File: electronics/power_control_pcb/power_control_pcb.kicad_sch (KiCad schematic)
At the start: 83 parts

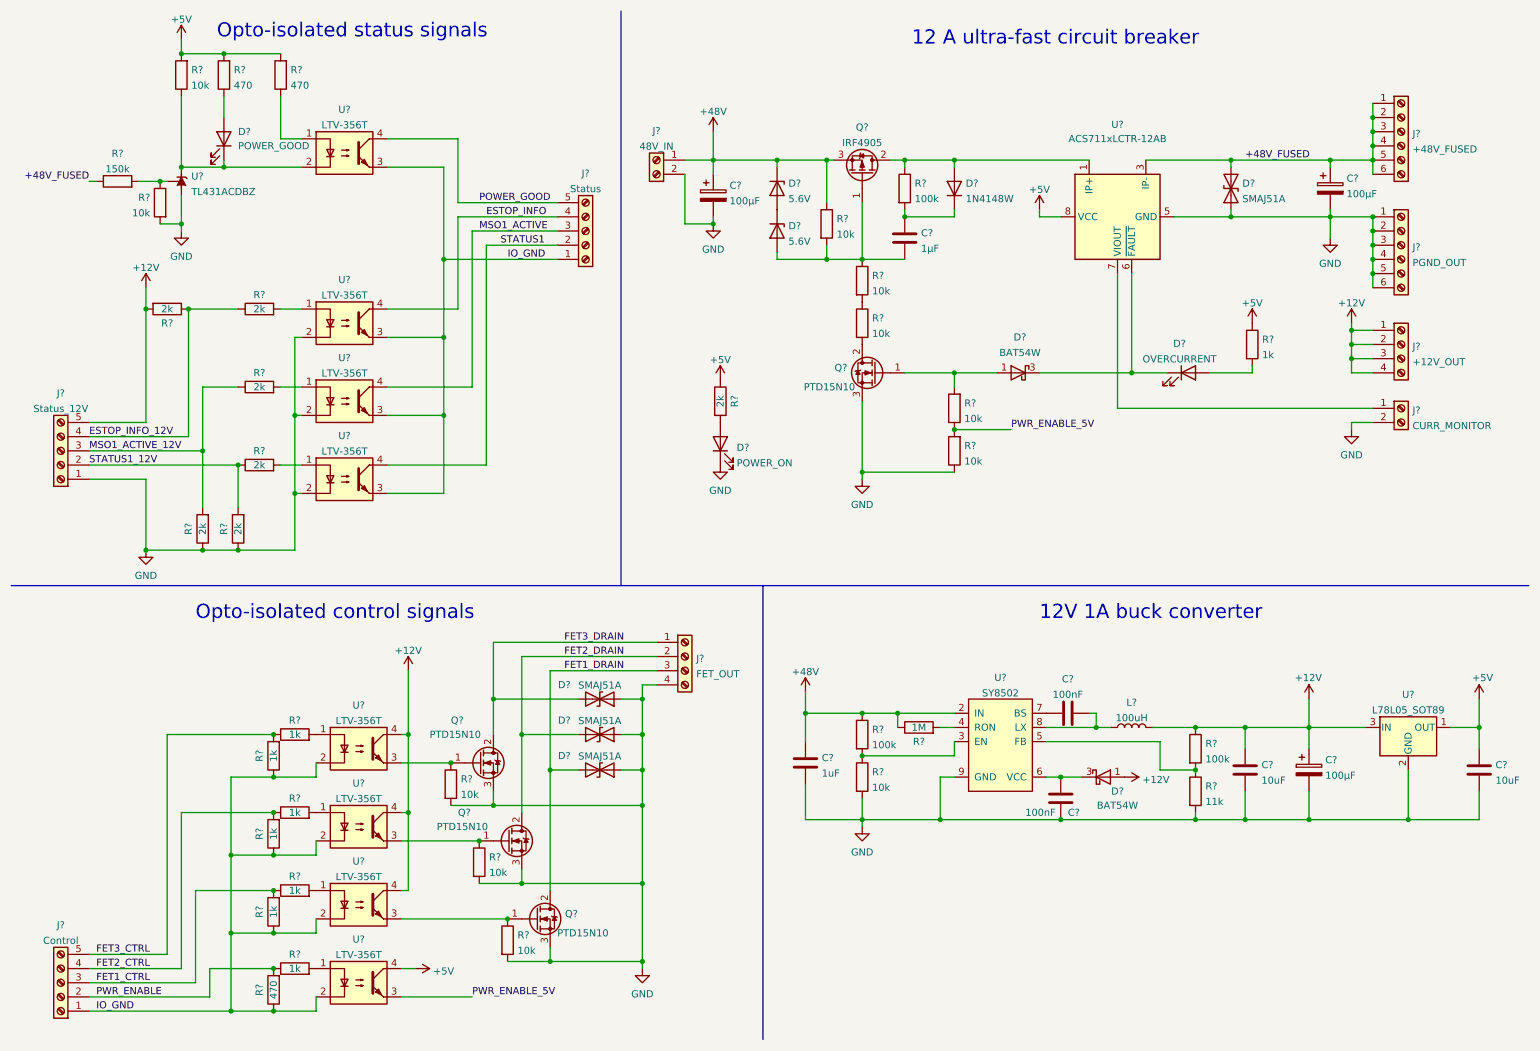
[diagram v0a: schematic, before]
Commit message: Update motor driver and power control PCB designs
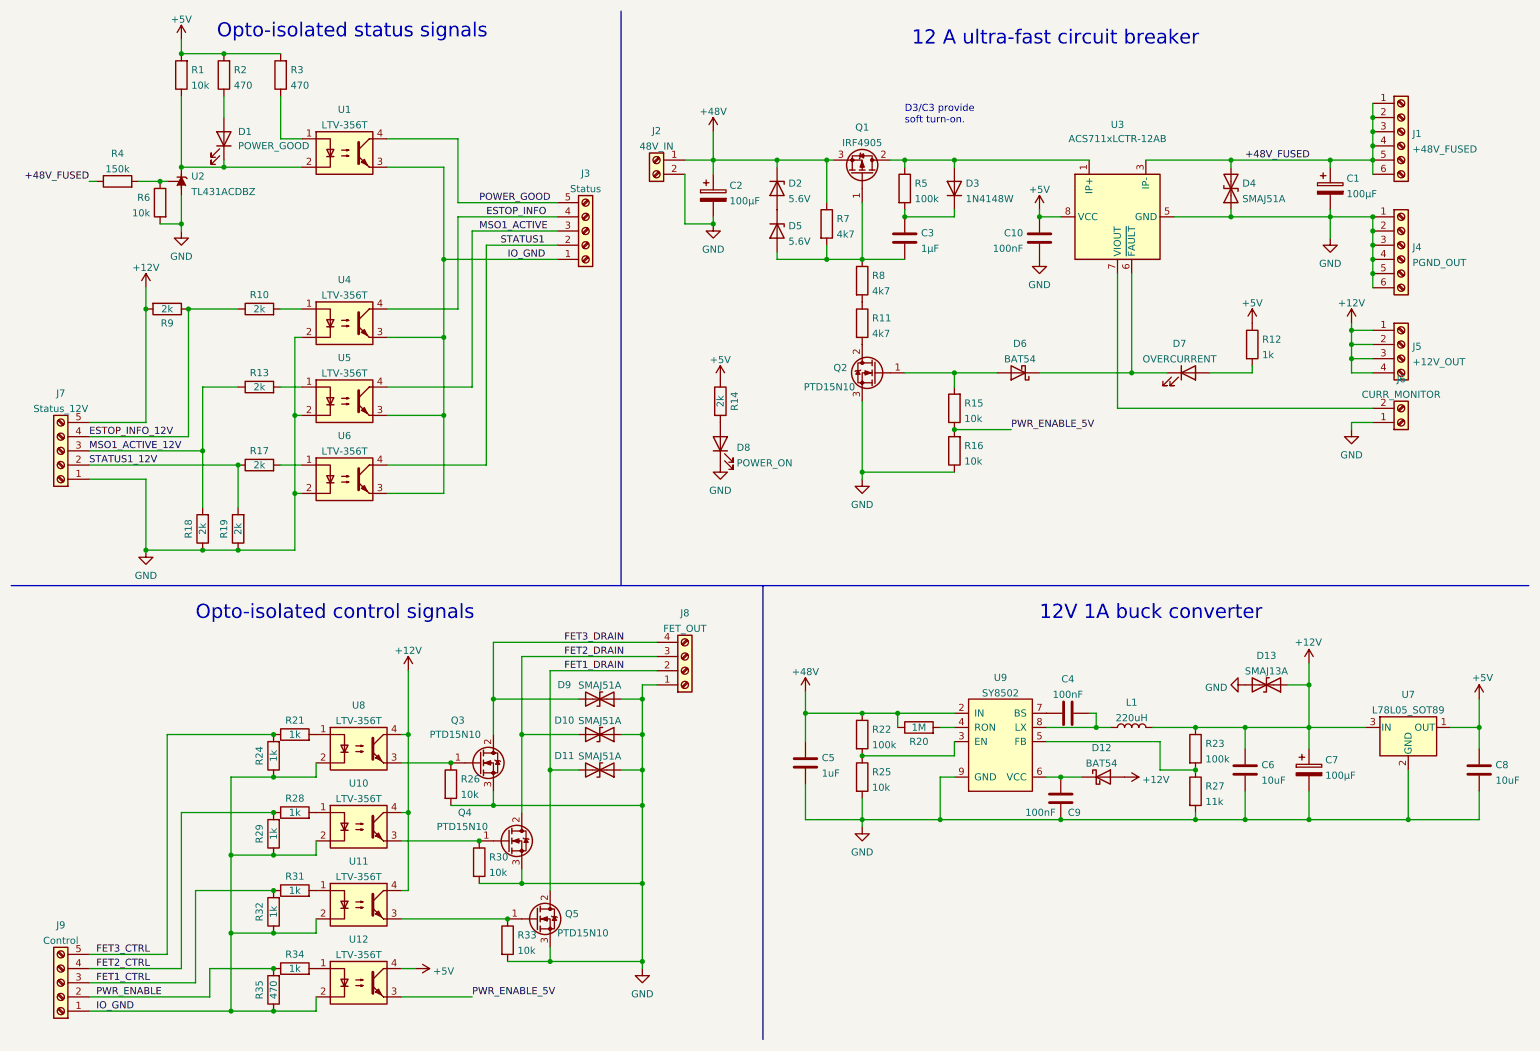
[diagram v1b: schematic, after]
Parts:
- removed D? (x2): BAT54W, Package_TO_SOT_SMD:SOT-323_SC-70, symbol Diode:BAT54W
- added C10: 100nF, Capacitor_SMD:C_0603_1608Metric, symbol Device:C
- added D12, D6: BAT54, Diode_SMD:D_SOD-123, symbol Device:D_Schottky
- added D13: SMAJ13A, Diode_SMD:D_SMA, symbol Device:D_TVS
- C1, C2, C7: renamed from C?; footprint (none) -> Capacitor_THT:CP_Radial_D10.0mm_P5.00mm
- C3, C5: renamed from C?; footprint (none) -> Capacitor_SMD:C_1210_3225Metric
- C4, C9: renamed from C?; footprint (none) -> Capacitor_SMD:C_0603_1608Metric
- C6, C8: renamed from C?; footprint (none) -> Capacitor_SMD:C_0805_2012Metric
- D1, D7, D8: renamed from D?; footprint (none) -> LED_THT:LED_D3.0mm
- D10, D11, D4, D9: renamed from D?; footprint (none) -> Diode_SMD:D_SMA
- D2, D5: renamed from D?; footprint (none) -> Diode_SMD:D_SOD-123
- J1, J4: renamed from J?; footprint (none) -> TerminalBlock_Phoenix:TerminalBlock_Phoenix_MKDS-1,5-6_1x06_P5.00mm_Horizontal
- J2, J6: renamed from J?; footprint (none) -> TerminalBlock_Phoenix:TerminalBlock_Phoenix_MKDS-1,5-2_1x02_P5.00mm_Horizontal
- J3, J7, J9: renamed from J?; footprint (none) -> TerminalBlock_TE-Connectivity:TerminalBlock_TE_282834-5_1x05_P2.54mm_Horizontal
- J5, J8: renamed from J?; footprint (none) -> TerminalBlock_Phoenix:TerminalBlock_Phoenix_MKDS-1,5-4_1x04_P5.00mm_Horizontal
- L1: renamed from L?; value 100uH -> 220uH; footprint (none) -> Inductor_SMD:L_12x12mm_H6mm
- Q1: renamed from Q?; footprint Package_TO_SOT_THT:TO-220-3_Vertical -> Package_TO_SOT_SMD:TO-263-3_TabPin2
- R1, R10, R12, R13, R14, R15, R16, R17, R18, R19, R2, R20, R21, R22, R23, R24, R25, R26, R27, R28, R29, R3, R30, R31, R32, R33, R34, R35, R4, R5, R6, R9: renamed from R?; footprint (none) -> Resistor_SMD:R_0603_1608Metric
- R11, R7, R8: renamed from R?; value 10k -> 4k7; footprint (none) -> Resistor_SMD:R_0603_1608Metric
- U9: renamed from U?; footprint (none) -> Package_SO:SOIC-8-1EP_3.9x4.9mm_P1.27mm_EP2.29x3mm
- gave numbers to parts that had none: 16
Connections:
- net +12V: now also D12.2 (A), D13.1 (A1)
- net +5V: now also C10.1
- net FET1_DRAIN: now also J8.2 (Pin_2); no longer J8.3 (Pin_3)
- net FET2_DRAIN: now also J8.3 (Pin_3); no longer J8.2 (Pin_2)
- net FET3_DRAIN: now also J8.4 (Pin_4); no longer J8.1 (Pin_1)
- net GND: now also J6.1 (Pin_1), J8.1 (Pin_1), C10.2, D13.2 (A2); no longer J6.2 (Pin_2), J8.4 (Pin_4)
- net at D7.1 (K), U3.6 (~{FAULT}): now also D6.1 (K)
- net at U3.7 (VIOUT): now also J6.2 (Pin_2); no longer J6.1 (Pin_1)
- net at C9.1, U9.6 (VCC): now also D12.1 (K)
- net at Q2.1 (G), R15.2: now also D6.2 (A)
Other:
- note added: "D3/C3 provide soft turn-on."
- company: (none) -> Hacklab Jyväskylä ry / Petteri Aimonen
- title: (none) -> CNC2 power control board

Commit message: Update wiring diagram & motor driver part values
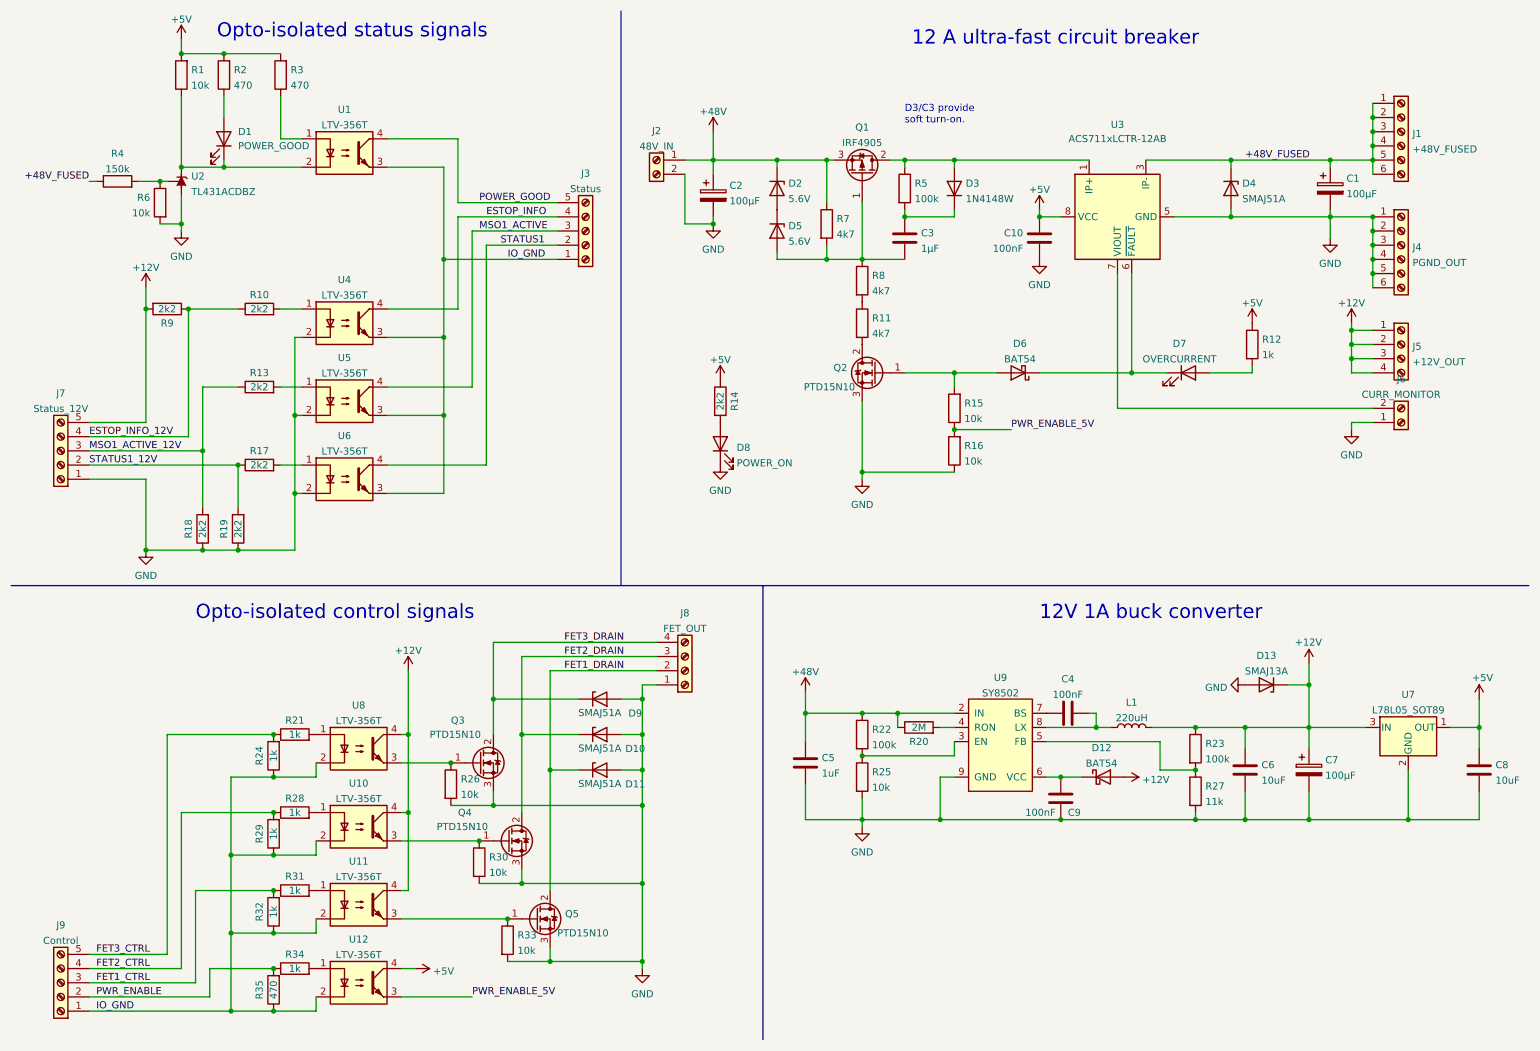
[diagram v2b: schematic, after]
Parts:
- D10, D11, D13, D4, D9: symbol Device:D_TVS -> Device:D_Zener
- R10, R13, R14, R17, R18, R19, R9: value 2k -> 2k2
- R20: value 1M -> 2M
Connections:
- net +48V_FUSED: now also D4.1 (K); no longer D4.2 (A2)
- net FET1_DRAIN: now also D11.1 (K); no longer D11.2 (A2)
- net FET2_DRAIN: now also D10.1 (K); no longer D10.2 (A2)
- net FET3_DRAIN: now also D9.1 (K); no longer D9.2 (A2)
- net GND: now also D10.2 (A), D11.2 (A), D4.2 (A), D9.2 (A); no longer D10.1 (A1), D11.1 (A1), D4.1 (A1), D9.1 (A1)
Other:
- moved on the sheet: D10, D11, D4, D9
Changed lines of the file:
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@@
     (in_bom yes) (on_board yes)
     (property "Reference" "R13" (id 0) (at 57.15 77.47 90))
-    (property "Value" "2k" (id 1) (at 57.15 80.01 90))
+    (property "Value" "2k2" (id 1) (at 57.15 80.01 90))
     (property "Footprint" "Resistor_SMD:R_0603_1608Metric" (id 2) (at 57.15 81.788 90)
       (effects (font (size 1.27 1.27)) hide)
@@
     (pin "3")
   )
-  (symbol (lib_id "Device:D_TVS") (at 231.14 44.45 90) (unit 1)
+  (symbol (lib_id "Device:D_Zener") (at 231.14 44.45 270) (unit 1)
     (in_bom yes) (on_board yes) (fields_autoplaced)
     (property "Reference" "D4" (id 0) (at 233.172 43.5415 90)
-      (effects (font (size 1.27 1.27)) (justify right))
+      (effects (font (size 1.27 1.27)) (justify left))
     )
     (property "Value" "SMAJ51A" (id 1) (at 233.172 46.3166 90)
-      (effects (font (size 1.27 1.27)) (justify right))
+      (effects (font (size 1.27 1.27)) (justify left))
     )
     (property "Footprint" "Diode_SMD:D_SMA" (id 2) (at 231.14 44.45 0)
@@
     (pin "3")
   )
-  (symbol (lib_id "Device:D_TVS") (at 118.11 148.59 180) (unit 1)
-    (in_bom yes) (on_board yes)
-    (property "Reference" "D11" (id 0) (at 111.76 146.05 0))
-    (property "Value" "SMAJ51A" (id 1) (at 118.11 146.1286 0))
+  (symbol (lib_id "Device:D_Zener") (at 118.11 148.59 0) (unit 1)
+    (in_bom yes) (on_board yes)
+    (property "Reference" "D11" (id 0) (at 124.46 151.13 0))
+    (property "Value" "SMAJ51A" (id 1) (at 118.11 151.0514 0))
     (property "Footprint" "Diode_SMD:D_SMA" (id 2) (at 118.11 148.59 0)
       (effects (font (size 1.27 1.27)) hide)
@@
     (in_bom yes) (on_board yes)
     (property "Reference" "R19" (id 0) (at 50.8 105.41 90))
-    (property "Value" "2k" (id 1) (at 53.34 105.41 90))
+    (property "Value" "2k2" (id 1) (at 53.34 105.41 90))
     (property "Footprint" "Resistor_SMD:R_0603_1608Metric" (id 2) (at 55.118 105.41 90)
       (effects (font (size 1.27 1.27)) hide)
@@
     (in_bom yes) (on_board yes)
     (property "Reference" "R14" (id 0) (at 142.24 82.55 90))
-    (property "Value" "2k" (id 1) (at 139.7 82.55 90))
+    (property "Value" "2k2" (id 1) (at 139.7 82.55 90))
     (property "Footprint" "Resistor_SMD:R_0603_1608Metric" (id 2) (at 137.922 82.55 90)
       (effects (font (size 1.27 1.27)) hide)
@@
     (in_bom yes) (on_board yes)
     (property "Reference" "R10" (id 0) (at 57.15 63.5 90))
-    (property "Value" "2k" (id 1) (at 57.15 66.04 90))
+    (property "Value" "2k2" (id 1) (at 57.15 66.04 90))
     (property "Footprint" "Resistor_SMD:R_0603_1608Metric" (id 2) (at 57.15 67.818 90)
       (effects (font (size 1.27 1.27)) hide)
@@
     (pin "4")
   )
-  (symbol (lib_id "Device:D_TVS") (at 237.49 133.35 180) (unit 1)
+  (symbol (lib_id "Device:D_Zener") (at 237.49 133.35 180) (unit 1)
     (in_bom yes) (on_board yes) (fields_autoplaced)
     (property "Reference" "D13" (id 0) (at 237.49 128.1135 0))
@@
     (in_bom yes) (on_board yes)
     (property "Reference" "R20" (id 0) (at 175.26 143.51 90))
-    (property "Value" "1M" (id 1) (at 175.26 140.97 90))
+    (property "Value" "2M" (id 1) (at 175.26 140.97 90))
     (property "Footprint" "Resistor_SMD:R_0603_1608Metric" (id 2) (at 175.26 142.748 90)
       (effects (font (size 1.27 1.27)) hide)
@@
     (pin "2")
   )
-  (symbol (lib_id "Device:D_TVS") (at 118.11 135.89 180) (unit 1)
-    (in_bom yes) (on_board yes)
-    (property "Reference" "D9" (id 0) (at 111.76 133.35 0))
-    (property "Value" "SMAJ51A" (id 1) (at 118.11 133.4286 0))
+  (symbol (lib_id "Device:D_Zener") (at 118.11 135.89 0) (unit 1)
+    (in_bom yes) (on_board yes)
+    (property "Reference" "D9" (id 0) (at 124.46 138.43 0))
+    (property "Value" "SMAJ51A" (id 1) (at 118.11 138.3514 0))
     (property "Footprint" "Diode_SMD:D_SMA" (id 2) (at 118.11 135.89 0)
       (effects (font (size 1.27 1.27)) hide)
@@
     (in_bom yes) (on_board yes)
     (property "Reference" "R9" (id 0) (at 40.64 68.58 90))
-    (property "Value" "2k" (id 1) (at 40.64 66.04 90))
+    (property "Value" "2k2" (id 1) (at 40.64 66.04 90))
     (property "Footprint" "Resistor_SMD:R_0603_1608Metric" (id 2) (at 40.64 64.262 90)
       (effects (font (size 1.27 1.27)) hide)
@@
     (pin "1")
   )
-  (symbol (lib_id "Device:D_TVS") (at 118.11 142.24 180) (unit 1)
-    (in_bom yes) (on_board yes)
-    (property "Reference" "D10" (id 0) (at 111.76 139.7 0))
-    (property "Value" "SMAJ51A" (id 1) (at 118.11 139.7786 0))
+  (symbol (lib_id "Device:D_Zener") (at 118.11 142.24 0) (unit 1)
+    (in_bom yes) (on_board yes)
+    (property "Reference" "D10" (id 0) (at 124.46 144.78 0))
+    (property "Value" "SMAJ51A" (id 1) (at 118.11 144.7014 0))
     (property "Footprint" "Diode_SMD:D_SMA" (id 2) (at 118.11 142.24 0)
       (effects (font (size 1.27 1.27)) hide)
@@
     (in_bom yes) (on_board yes)
     (property "Reference" "R18" (id 0) (at 44.45 105.41 90))
-    (property "Value" "2k" (id 1) (at 46.99 105.41 90))
+    (property "Value" "2k2" (id 1) (at 46.99 105.41 90))
     (property "Footprint" "Resistor_SMD:R_0603_1608Metric" (id 2) (at 48.768 105.41 90)
       (effects (font (size 1.27 1.27)) hide)
@@
     (in_bom yes) (on_board yes)
     (property "Reference" "R17" (id 0) (at 57.15 91.44 90))
-    (property "Value" "2k" (id 1) (at 57.15 93.98 90))
+    (property "Value" "2k2" (id 1) (at 57.15 93.98 90))
     (property "Footprint" "Resistor_SMD:R_0603_1608Metric" (id 2) (at 57.15 95.758 90)
       (effects (font (size 1.27 1.27)) hide)
@@
     )
     (path "/d8545924-c3bc-43c9-933b-3ff44d05181f"
-      (reference "R9") (unit 1) (value "2k") (footprint "Resistor_SMD:R_0603_1608Metric")
+      (reference "R9") (unit 1) (value "2k2") (footprint "Resistor_SMD:R_0603_1608Metric")
     )
     (path "/a6ab0791-dac8-4cd2-b0d5-fcc16ada43d3"
-      (reference "R10") (unit 1) (value "2k") (footprint "Resistor_SMD:R_0603_1608Metric")
+      (reference "R10") (unit 1) (value "2k2") (footprint "Resistor_SMD:R_0603_1608Metric")
     )
     (path "/1004a736-debf-46e8-b5c1-3e63797c62c1"
@@
     )
     (path "/0a43b64d-1c7a-4e06-8181-946a35ed5c85"
-      (reference "R13") (unit 1) (value "2k") (footprint "Resistor_SMD:R_0603_1608Metric")
+      (reference "R13") (unit 1) (value "2k2") (footprint "Resistor_SMD:R_0603_1608Metric")
     )
     (path "/a0829975-9b8e-46e1-833b-08818166012a"
-      (reference "R14") (unit 1) (value "2k") (footprint "Resistor_SMD:R_0603_1608Metric")
+      (reference "R14") (unit 1) (value "2k2") (footprint "Resistor_SMD:R_0603_1608Metric")
     )
     (path "/eccffa0a-7175-4588-b0cb-f971a9b25ae9"
@@
     )
     (path "/f1747de2-9aae-42d0-8510-da7938be2dfb"
-      (reference "R17") (unit 1) (value "2k") (footprint "Resistor_SMD:R_0603_1608Metric")
+      (reference "R17") (unit 1) (value "2k2") (footprint "Resistor_SMD:R_0603_1608Metric")
     )
     (path "/e948ac92-4538-4483-8cd2-46d0f1980022"
-      (reference "R18") (unit 1) (value "2k") (footprint "Resistor_SMD:R_0603_1608Metric")
+      (reference "R18") (unit 1) (value "2k2") (footprint "Resistor_SMD:R_0603_1608Metric")
     )
     (path "/961bafc9-0776-4fab-8dbe-383f8965f14b"
-      (reference "R19") (unit 1) (value "2k") (footprint "Resistor_SMD:R_0603_1608Metric")
+      (reference "R19") (unit 1) (value "2k2") (footprint "Resistor_SMD:R_0603_1608Metric")
     )
     (path "/c01122f7-a463-421d-a3c1-7a63dafcd857"
-      (reference "R20") (unit 1) (value "1M") (footprint "Resistor_SMD:R_0603_1608Metric")
+      (reference "R20") (unit 1) (value "2M") (footprint "Resistor_SMD:R_0603_1608Metric")
     )
     (path "/75680ac7-e730-46c6-90f3-df8086f0846b"
